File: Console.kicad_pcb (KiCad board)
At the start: 2 copper layers, 59.6 x 60.4 mm, 61 parts, among them J1 batt_in, J11 lcd_out, J14 gnd_out, J17 node_conn_1, J18 node_conn_2, J2 3v3_gnd, J3 motor_out, J4 ir_out, J5 pwr_jumper, J6 gpio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

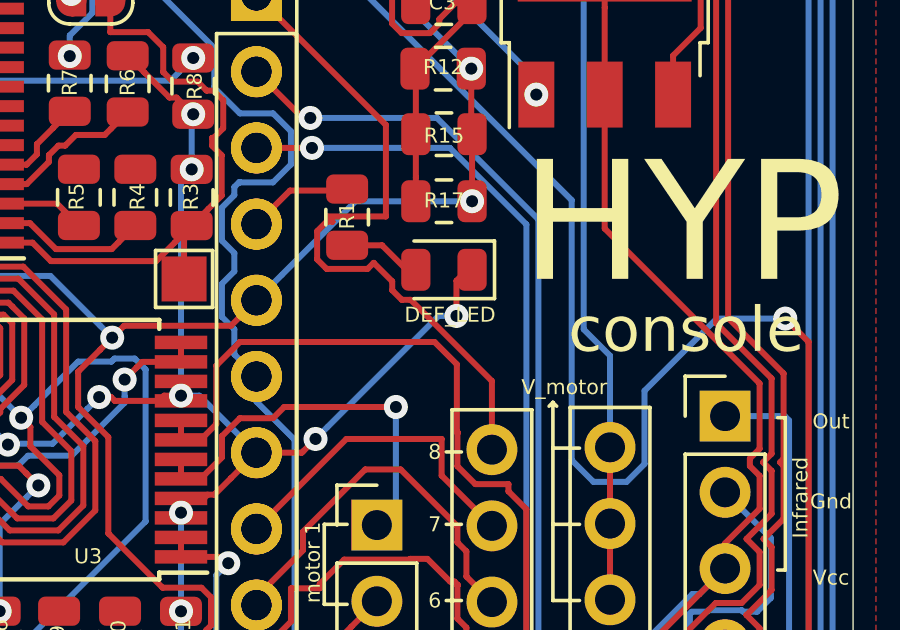
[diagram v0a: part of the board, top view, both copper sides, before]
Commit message: Add Busy LED
Changed the DEF_LED to BSY_LED to indicate network business. The default led in the breakout board remains the same.
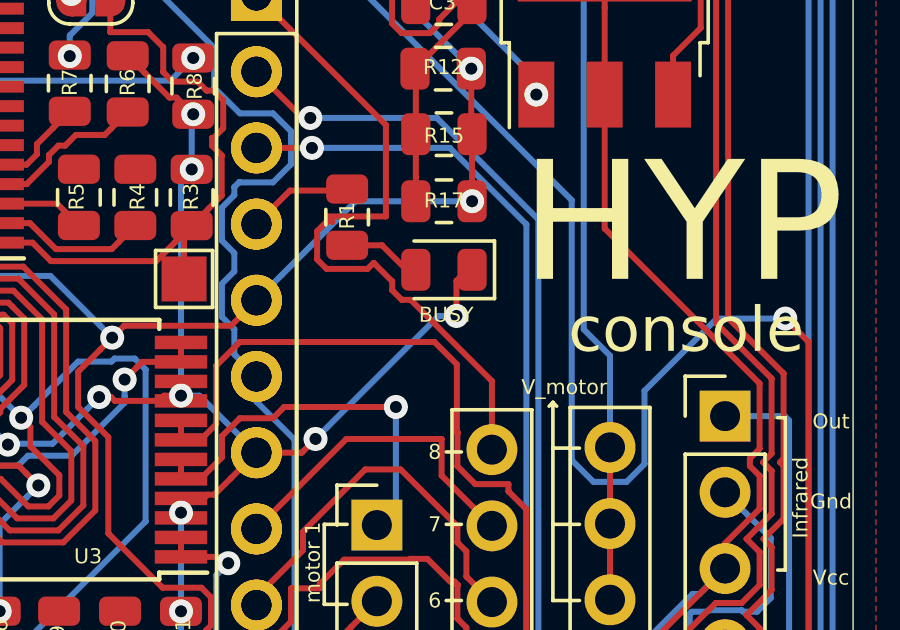
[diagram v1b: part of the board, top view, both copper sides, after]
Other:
- board text added: "BUSY"
- board text removed: "DEF_LED"
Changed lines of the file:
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@@
     (effects (font (size 0.5 0.5) (thickness 0.12)))
   )
-  (gr_text DEF_LED (at 104.013 57.023) (layer F.SilkS)
+  (gr_text BUSY (at 103.886 57.023) (layer F.SilkS)
     (effects (font (size 0.5 0.5) (thickness 0.12)))
   )
